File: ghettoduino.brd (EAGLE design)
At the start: 50 x 19.3 mm, 13 parts

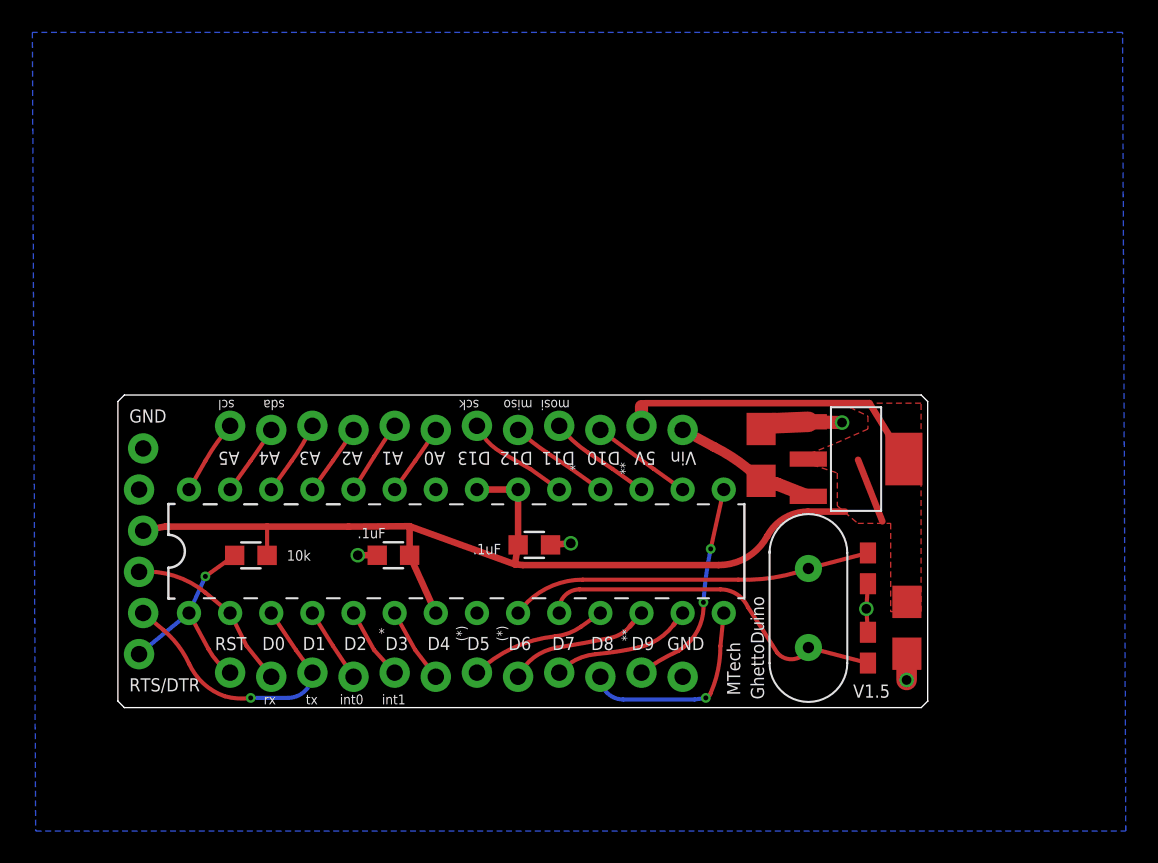
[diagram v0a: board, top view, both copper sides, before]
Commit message: Added p-channel MOSFET for reverse power protection.
Gerber, eps files still need update.
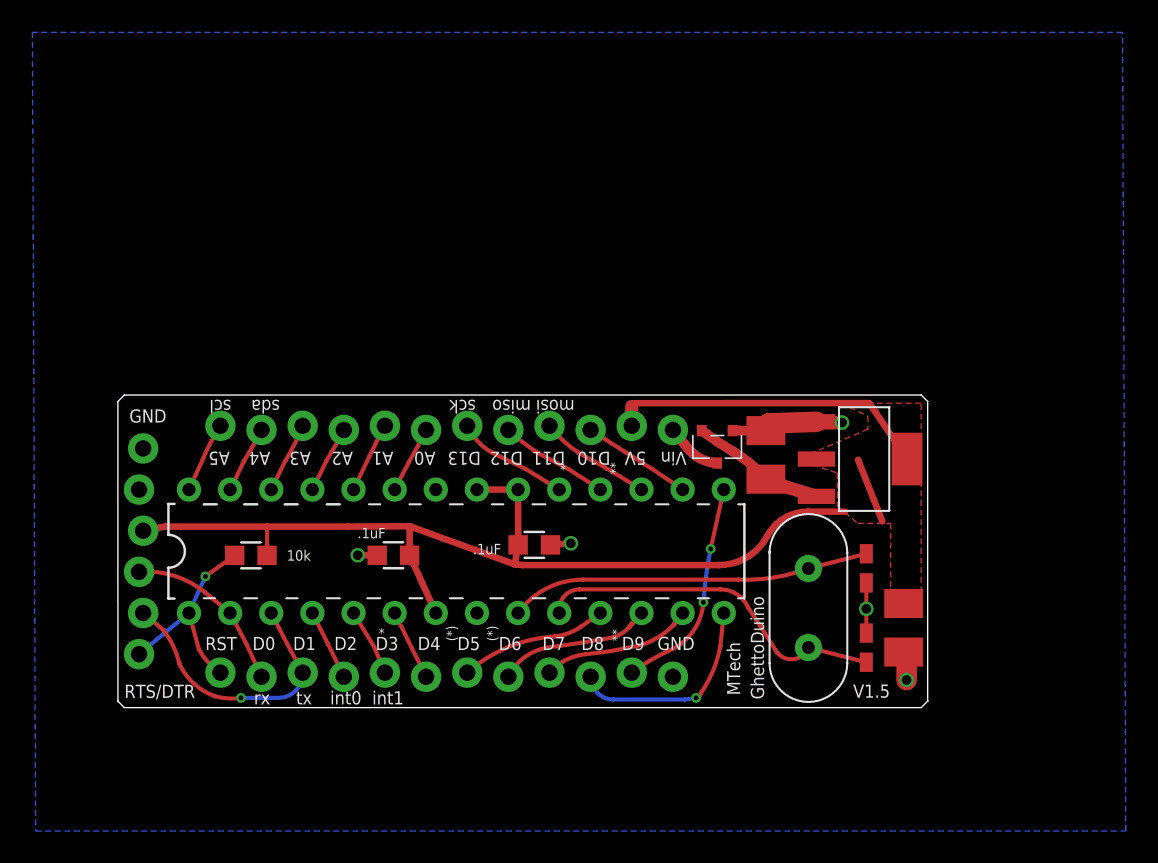
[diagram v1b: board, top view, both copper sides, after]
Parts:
- added U$3: P-MOSFET-PMV48XP, 1dah:SOT23-3LEAD
- 5V: value ZLDO1117 -> 5V-LDO-ZLDO1117
- moved U$2 0.60 mm to (6.33, 2.03)
- moved U$5 0.60 mm to (6.33, 17.3)
- moved 5V 0.50 mm to (46.1, 15.3)
- moved C8 0.30 mm to (40.0, 15.6)
- moved C5 0.20 mm to (48.5, 4.93)
- moved C1 0.10 mm to (46.2, 8.60)
- moved C3 0.10 mm to (46.2, 3.70)
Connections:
- new net N$1: U$3.3, U$5.12
- net GND: now also U$3.1
- net VIN: now also U$3.2; no longer U$5.12
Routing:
- net N$1: track 0.00 -> 3.49 mm
- net GND: track 12.2 -> 14.4 mm
- net 5V: track 82.8 -> 83.5 mm
- net D1: track 17.8 -> 17.2 mm
- net VIN: track 8.86 -> 8.27 mm
- net D6: track 8.85 -> 9.44 mm
- net D5: track 8.49 -> 9.04 mm
- net D7: track 8.70 -> 9.22 mm
- net D13: track 6.48 -> 7.00 mm
- net D12: track 6.28 -> 6.79 mm
- net D11: track 6.44 -> 6.95 mm

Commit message: Added p-FET reverse bias protection, more markings, extra ground pin, general re-arranging and cleanup.
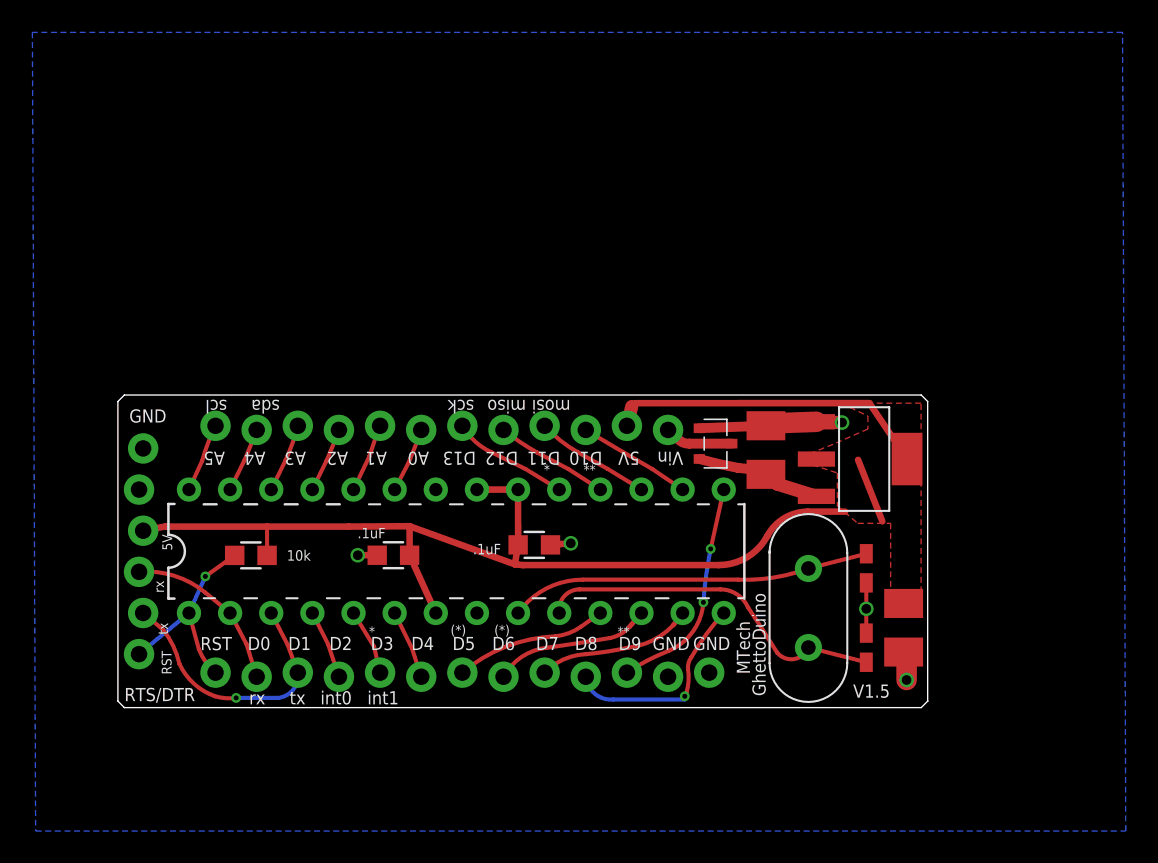
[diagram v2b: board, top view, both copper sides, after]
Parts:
- U$2: device 1dah:1X12_LOCK -> 1dah:1X13_LOCK
- moved C8 0.30 mm to (40.0, 15.9)
- moved U$2 0.30 mm to (6.03, 2.03)
- moved U$5 0.30 mm to (6.03, 17.3)
- moved U$3 0.22 mm to (36.9, 16.3), turned to 90 degrees
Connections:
- net GND: now also U$2.13
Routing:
- net GND: track 14.4 -> 16.2 mm
- net N$1: track 3.49 -> 4.19 mm
- net VIN: track 8.27 -> 7.67 mm
